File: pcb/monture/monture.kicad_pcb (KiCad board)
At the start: 2 copper layers, 110 x 85 mm, 13 parts, among them U1 Teensy 4.1

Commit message: feat(pcb): integration physique de l'ecran LCD 2004/1602 avec entretoises M3 sur le PCB de la raquette
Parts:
- H1, H2, H3, H4: value M3 -> Fixation Boitier M3

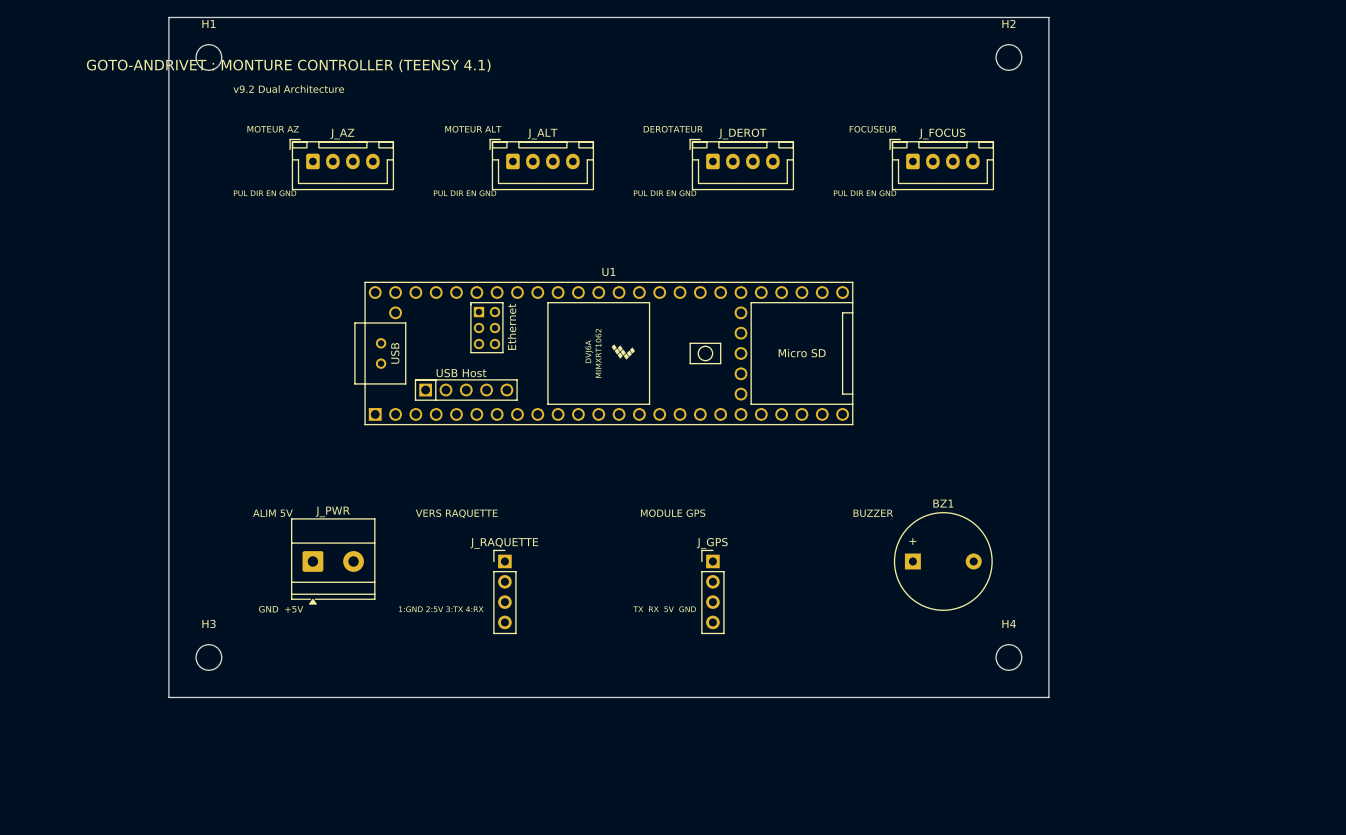
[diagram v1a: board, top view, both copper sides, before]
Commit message: feat(pcb): passage en 36V haute puissance, integration de 4 drivers 4A TMC5160, convertisseur buck 36V->5V et borniers directs moteurs
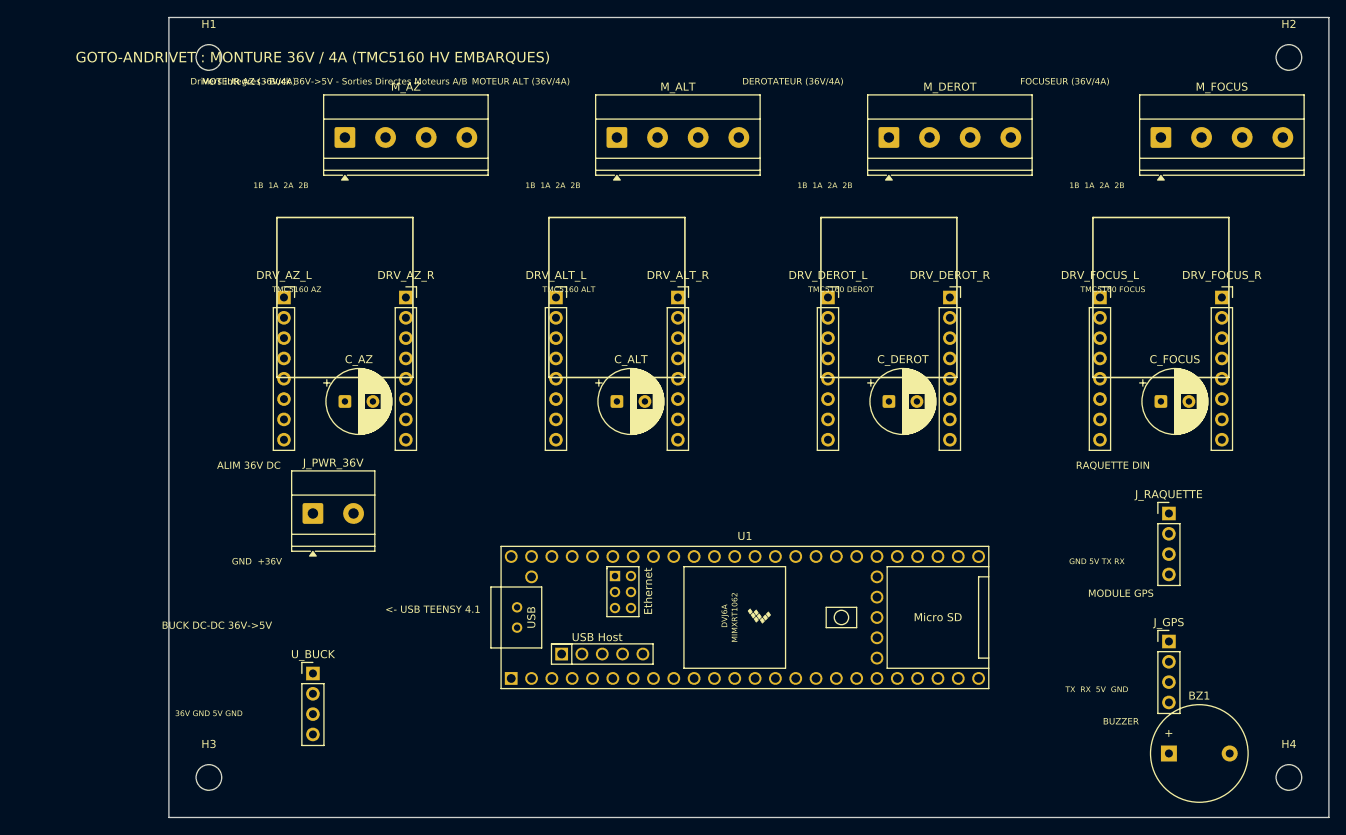
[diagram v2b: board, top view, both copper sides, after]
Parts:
- removed J_ALT: MOTEUR ALT, JST_XH_B4B-XH-A_1x04_P2.50mm_Vertical
- removed J_AZ: MOTEUR AZ, JST_XH_B4B-XH-A_1x04_P2.50mm_Vertical
- removed J_DEROT: DEROTATEUR, JST_XH_B4B-XH-A_1x04_P2.50mm_Vertical
- removed J_FOCUS: FOCUSEUR, JST_XH_B4B-XH-A_1x04_P2.50mm_Vertical
- removed J_PWR: ALIM 5V, TerminalBlock_Phoenix_MKDS-1,5-2-5.08_1x02_P5.08mm_Horizontal
- added C_ALT: 470uF 50V/63V, CP_Radial_D8.0mm_P3.50mm, F.Cu at (56.0, 48.0)
- added C_AZ: 470uF 50V/63V, CP_Radial_D8.0mm_P3.50mm, F.Cu at (22.0, 48.0)
- added C_DEROT: 470uF 50V/63V, CP_Radial_D8.0mm_P3.50mm, F.Cu at (90.0, 48.0)
- added C_FOCUS: 470uF 50V/63V, CP_Radial_D8.0mm_P3.50mm, F.Cu at (124.0, 48.0)
- added DRV_ALT_L: Logique, PinSocket_1x08_P2.54mm_Vertical, F.Cu at (48.4, 35.0)
- added DRV_ALT_R: Puissance, PinSocket_1x08_P2.54mm_Vertical, F.Cu at (63.6, 35.0)
- added DRV_AZ_L: Logique, PinSocket_1x08_P2.54mm_Vertical, F.Cu at (14.4, 35.0)
- added DRV_AZ_R: Puissance, PinSocket_1x08_P2.54mm_Vertical, F.Cu at (29.6, 35.0)
- added DRV_DEROT_L: Logique, PinSocket_1x08_P2.54mm_Vertical, F.Cu at (82.4, 35.0)
- added DRV_DEROT_R: Puissance, PinSocket_1x08_P2.54mm_Vertical, F.Cu at (97.6, 35.0)
- added DRV_FOCUS_L: Logique, PinSocket_1x08_P2.54mm_Vertical, F.Cu at (116.4, 35.0)
- added DRV_FOCUS_R: Puissance, PinSocket_1x08_P2.54mm_Vertical, F.Cu at (131.6, 35.0)
- added J_PWR_36V: ALIM 36V DC, TerminalBlock_Phoenix_MKDS-1,5-2-5.08_1x02_P5.08mm_Horizontal, F.Cu at (18.0, 62.0)
- added M_ALT: MOTEUR ALT, TerminalBlock_Phoenix_MKDS-1,5-4-5.08_1x04_P5.08mm_Horizontal, F.Cu at (56.0, 15.0)
- added M_AZ: MOTEUR AZ, TerminalBlock_Phoenix_MKDS-1,5-4-5.08_1x04_P5.08mm_Horizontal, F.Cu at (22.0, 15.0)
- added M_DEROT: MOTEUR DEROT, TerminalBlock_Phoenix_MKDS-1,5-4-5.08_1x04_P5.08mm_Horizontal, F.Cu at (90.0, 15.0)
- added M_FOCUS: MOTEUR FOCUS, TerminalBlock_Phoenix_MKDS-1,5-4-5.08_1x04_P5.08mm_Horizontal, F.Cu at (124.0, 15.0)
- added U_BUCK: Buck 36V->5V, PinHeader_1x04_P2.54mm_Vertical, F.Cu at (18.0, 82.0)
- H1, H2, H3, H4: value Fixation Boitier M3 -> M3 Fixation
- J_RAQUETTE: value RAQUETTE DIN -> VERS RAQUETTE
- moved J_RAQUETTE 83.2 mm to (125.0, 62.0)
- moved J_GPS 57.9 mm to (125.0, 78.0)
- moved BZ1 40.0 mm to (125.0, 92.0)
- moved H4 38.1 mm to (140.0, 95.0)
- moved U1 37.1 mm to (72.0, 75.0)
- moved H2 35.0 mm to (140.0, 5.00)
- moved H3 15.0 mm to (5.00, 95.0)
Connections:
- U1 pad 10: DEROT_PUL -> DEROT_STEP
- U1 pad 13: FOCUS_PUL -> FOCUS_STEP
- U1 pad 4: AZ_PUL -> AZ_STEP
- U1 pad 7: ALT_PUL -> ALT_STEP
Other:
- board size 110 x 85 mm -> 145 x 100 mm
- board text added: "1B 1A 2A 2B"
- board text added: "36V GND 5V GND"
- board text added: "<- USB TEENSY 4.1"
- board text added: "ALIM 36V DC"
- board text added: "BUCK DC-DC 36V->5V"
- board text added: "DEROTATEUR (36V/4A)"
- board text added: "Drivers integres - Buck 36V->5V - Sorties Directes Moteurs A/B"
- board text added: "FOCUSEUR (36V/4A)"
- board text added: "GND +36V"
- board text added: "GND 5V TX RX"
- board text added: "GOTO-ANDRIVET : MONTURE 36V / 4A (TMC5160 HV EMBARQUES)"
- board text added: "MOTEUR ALT (36V/4A)"
- board text added: "MOTEUR AZ (36V/4A)"
- board text added: "RAQUETTE DIN"
- board text added: "TMC5160 ALT"
- board text added: "TMC5160 AZ"
- board text added: "TMC5160 DEROT"
- board text added: "TMC5160 FOCUS"
- board text removed: "1:GND 2:5V 3:TX 4:RX"
- board text removed: "ALIM 5V"
- board text removed: "DEROTATEUR"
- board text removed: "FOCUSEUR"
- board text removed: "GND +5V"
- board text removed: "GOTO-ANDRIVET : MONTURE CONTROLLER (TEENSY 4.1)"
- board text removed: "MOTEUR ALT"
- board text removed: "MOTEUR AZ"
- board text removed: "PUL DIR EN GND"
- board text removed: "VERS RAQUETTE"
- board text removed: "v9.2 Dual Architecture"

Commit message: feat(pcb): ajout du regulateur de decoupage 36V->5V visible avec condensateurs et empreinte step-down LM2596HV
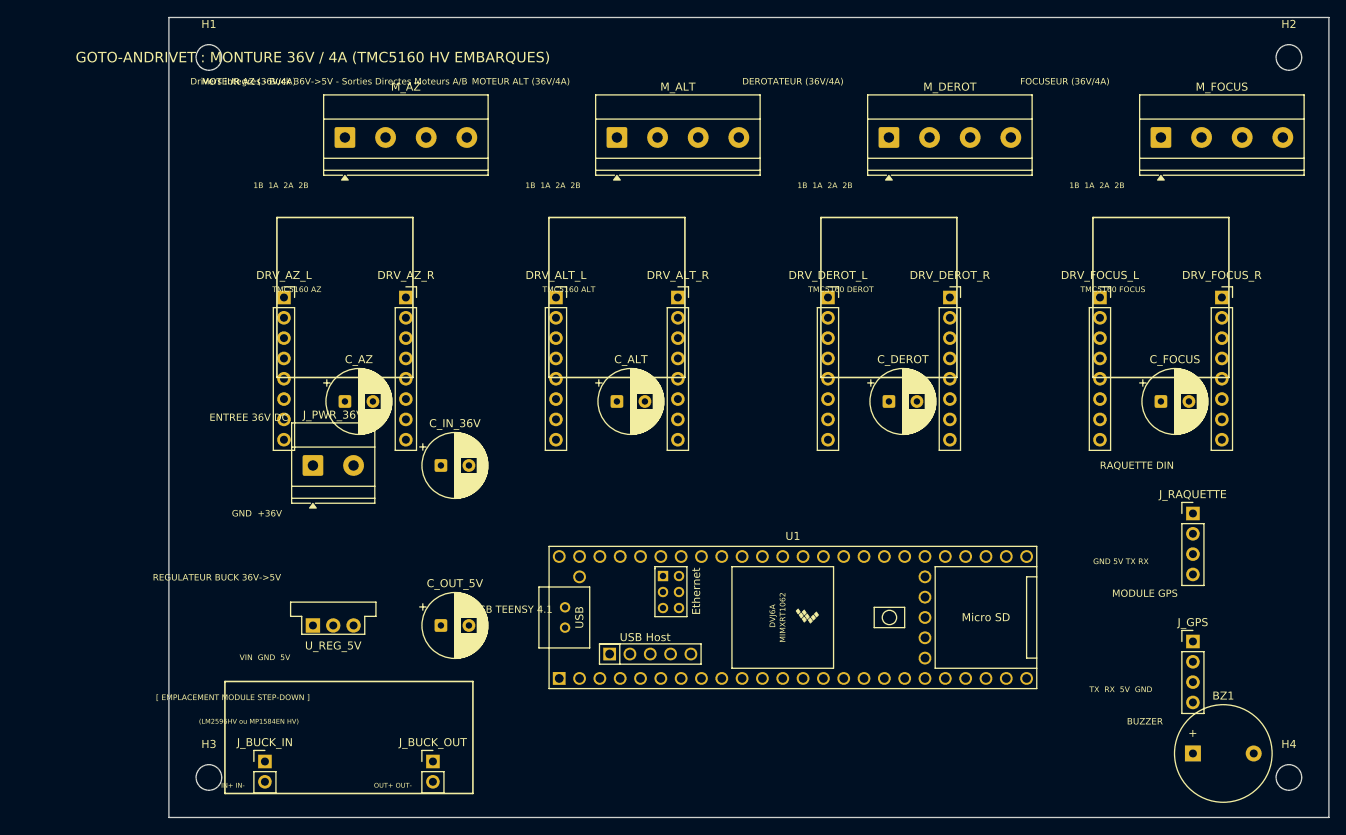
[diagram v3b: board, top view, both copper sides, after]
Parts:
- removed U_BUCK: Buck 36V->5V, PinHeader_1x04_P2.54mm_Vertical
- added C_IN_36V: 100uF 50V, CP_Radial_D8.0mm_P3.50mm, F.Cu at (34.0, 56.0)
- added C_OUT_5V: 220uF 16V, CP_Radial_D8.0mm_P3.50mm, F.Cu at (34.0, 76.0)
- added J_BUCK_IN: IN 36V/GND, PinHeader_1x02_P2.54mm_Vertical, F.Cu at (12.0, 93.0)
- added J_BUCK_OUT: OUT 5V/GND, PinHeader_1x02_P2.54mm_Vertical, F.Cu at (33.0, 93.0)
- added U_REG_5V: Buck 36V->5V, Converter_DCDC_Murata_OKI-78SR_Vertical, F.Cu at (18.0, 76.0)
- moved J_PWR_36V 6.00 mm to (18.0, 56.0)
- moved U1 6.00 mm to (78.0, 75.0)
- moved BZ1 3.00 mm to (128.0, 92.0)
- moved J_GPS 3.00 mm to (128.0, 78.0)
- moved J_RAQUETTE 3.00 mm to (128.0, 62.0)
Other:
- board text added: "(LM2596HV ou MP1584EN HV)"
- board text added: "ENTREE 36V DC"
- board text added: "IN+ IN-"
- board text added: "OUT+ OUT-"
- board text added: "REGULATEUR BUCK 36V->5V"
- board text added: "VIN GND 5V"
- board text added: "[ EMPLACEMENT MODULE STEP-DOWN ]"
- board text removed: "36V GND 5V GND"
- board text removed: "ALIM 36V DC"
- board text removed: "BUCK DC-DC 36V->5V"

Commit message: feat(pcb): orientation de tous les connecteurs et borniers vers l exterieur du PCB
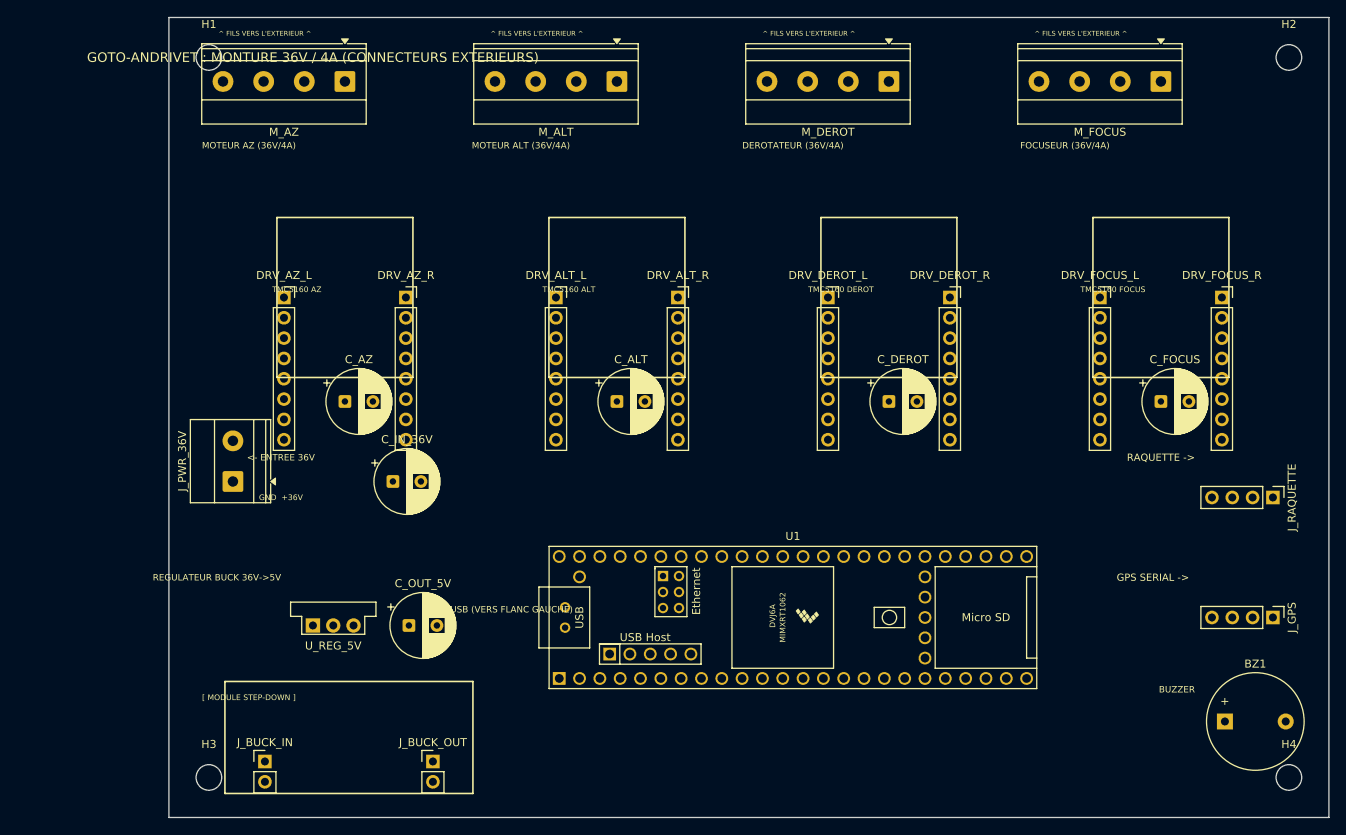
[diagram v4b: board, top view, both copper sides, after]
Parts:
- J_BUCK_IN: value IN 36V/GND -> IN 36V
- J_BUCK_OUT: value OUT 5V/GND -> OUT 5V
- moved J_GPS 10.4 mm to (138.0, 75.0), turned to -90 degrees
- moved J_PWR_36V 10.2 mm to (8.00, 58.0), turned to 90 degrees
- moved J_RAQUETTE 10.2 mm to (138.0, 60.0), turned to -90 degrees
- moved M_ALT 7.00 mm to (56.0, 8.00), turned to 180 degrees
- moved M_AZ 7.00 mm to (22.0, 8.00), turned to 180 degrees
- moved M_DEROT 7.00 mm to (90.0, 8.00), turned to 180 degrees
- moved M_FOCUS 7.00 mm to (124.0, 8.00), turned to 180 degrees
- moved C_IN_36V 6.32 mm to (28.0, 58.0)
- moved BZ1 5.66 mm to (132.0, 88.0)
- moved C_OUT_5V 4.00 mm to (30.0, 76.0)
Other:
- board text added: "<- ENTREE 36V"
- board text added: "<- USB (VERS FLANC GAUCHE)"
- board text added: "GOTO-ANDRIVET : MONTURE 36V / 4A (CONNECTEURS EXTERIEURS)"
- board text added: "GPS SERIAL ->"
- board text added: "RAQUETTE ->"
- board text added: "[ MODULE STEP-DOWN ]"
- board text added: "^ FILS VERS L'EXTERIEUR ^"
- board text removed: "(LM2596HV ou MP1584EN HV)"
- board text removed: "1B 1A 2A 2B"
- board text removed: "<- USB TEENSY 4.1"
- board text removed: "Drivers integres - Buck 36V->5V - Sorties Directes Moteurs A/B"
- board text removed: "ENTREE 36V DC"
- board text removed: "GND 5V TX RX"
- board text removed: "GOTO-ANDRIVET : MONTURE 36V / 4A (TMC5160 HV EMBARQUES)"
- board text removed: "IN+ IN-"
- board text removed: "MODULE GPS"
- board text removed: "OUT+ OUT-"
- board text removed: "RAQUETTE DIN"
- board text removed: "TX RX 5V GND"
- board text removed: "VIN GND 5V"
- board text removed: "[ EMPLACEMENT MODULE STEP-DOWN ]"

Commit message: feat(pcb): integration 100% discrete du circuit Buck 36V->5V sur le PCB (LM2596-5.0, diode 1N5822, inductance 33uH)
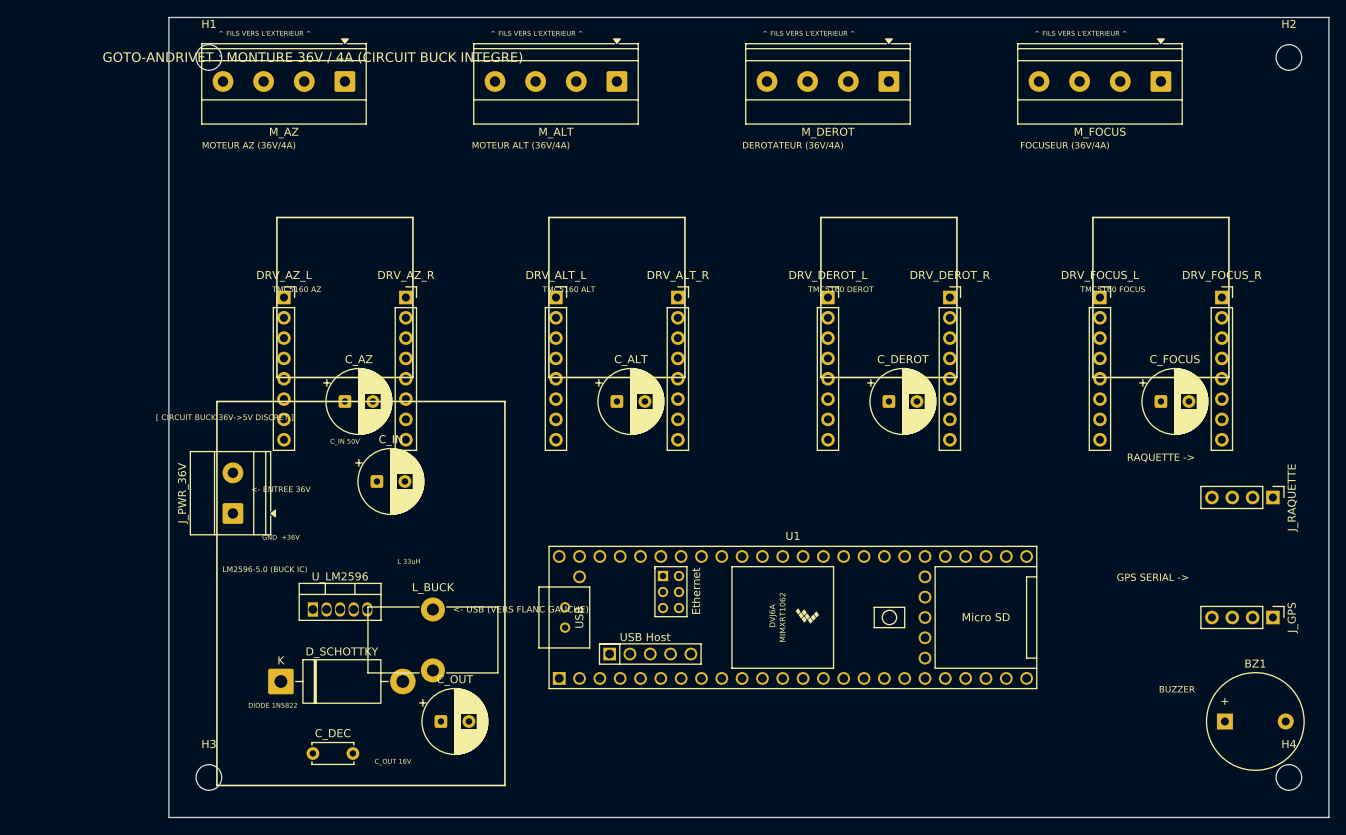
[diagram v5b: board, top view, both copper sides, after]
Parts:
- removed C_IN_36V: 100uF 50V, CP_Radial_D8.0mm_P3.50mm
- removed C_OUT_5V: 220uF 16V, CP_Radial_D8.0mm_P3.50mm
- removed J_BUCK_IN: IN 36V, PinHeader_1x02_P2.54mm_Vertical
- removed J_BUCK_OUT: OUT 5V, PinHeader_1x02_P2.54mm_Vertical
- removed U_REG_5V: Buck 36V->5V, Converter_DCDC_Murata_OKI-78SR_Vertical
- added C_DEC: 100nF, C_Disc_D5.0mm_W2.5mm_P5.00mm, F.Cu at (18.0, 92.0)
- added C_IN: 100uF 50V, CP_Radial_D8.0mm_P3.50mm, F.Cu at (26.0, 58.0)
- added C_OUT: 470uF 16V, CP_Radial_D8.0mm_P3.50mm, F.Cu at (34.0, 88.0)
- added D_SCHOTTKY: 1N5822 (3A), D_DO-201AD_P15.24mm_Horizontal, F.Cu at (14.0, 83.0)
- added L_BUCK: 33uH-47uH 3A, L_Toroid_Vertical_L16.0mm_W8.0mm_P7.62mm, F.Cu at (33.0, 74.0)
- added U_LM2596: LM2596-5.0, TO-220-5_Vertical, F.Cu at (18.0, 74.0)
- moved J_PWR_36V 4.00 mm to (8.00, 62.0)
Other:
- board text added: "C_IN 50V"
- board text added: "C_OUT 16V"
- board text added: "DIODE 1N5822"
- board text added: "GOTO-ANDRIVET : MONTURE 36V / 4A (CIRCUIT BUCK INTEGRE)"
- board text added: "L 33uH"
- board text added: "LM2596-5.0 (BUCK IC)"
- board text added: "[ CIRCUIT BUCK 36V->5V DISCRET ]"
- board text removed: "GOTO-ANDRIVET : MONTURE 36V / 4A (CONNECTEURS EXTERIEURS)"
- board text removed: "REGULATEUR BUCK 36V->5V"
- board text removed: "[ MODULE STEP-DOWN ]"
